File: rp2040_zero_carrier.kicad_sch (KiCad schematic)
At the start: 17 parts, among them J1 LPC, J2 SPARE, J5 EXP, J6 LCD, J7 UART

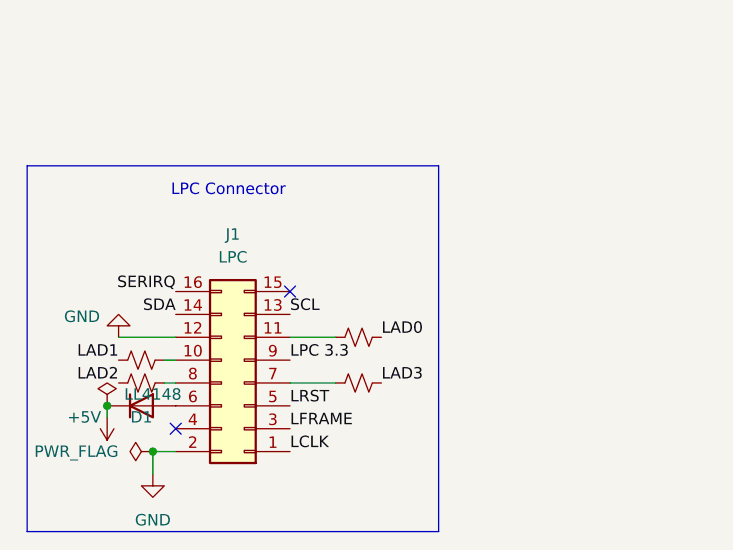
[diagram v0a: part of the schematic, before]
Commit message: Updated rp2040 zero footprint
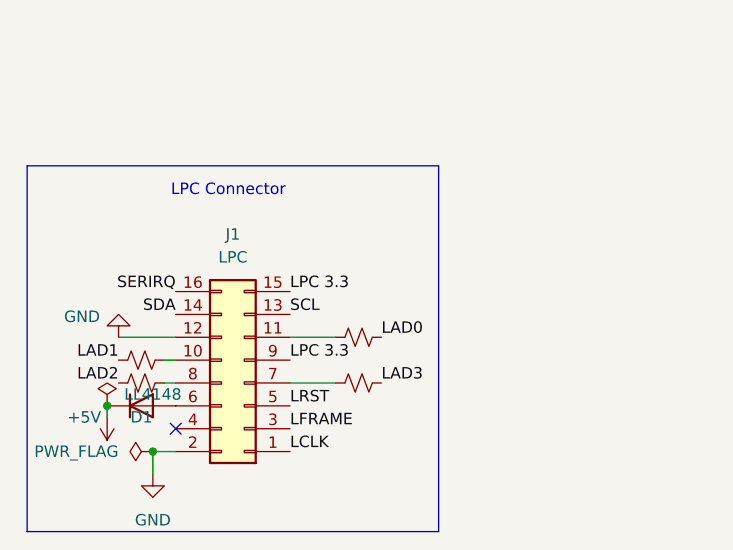
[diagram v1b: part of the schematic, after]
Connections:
- net LPC 3.3: now also J1.15 (Pin_15)
- no-connect marks 2 -> 1
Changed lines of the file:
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@@
-	)
-	(no_connect
-		(at 41.91 170.18)
 	)
 	(no_connect
@@
 		(fields_autoplaced yes)
 		(effects
+			(font
+				(size 1.27 1.27)
+			)
+			(justify left bottom)
+		)
+	)
+	(label "LPC 3.3"
+		(at 41.91 170.18 0)
+		(fields_autoplaced yes)
+		(effects
